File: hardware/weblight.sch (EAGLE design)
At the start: 15 parts, among them U1 ATtiny85-20SU

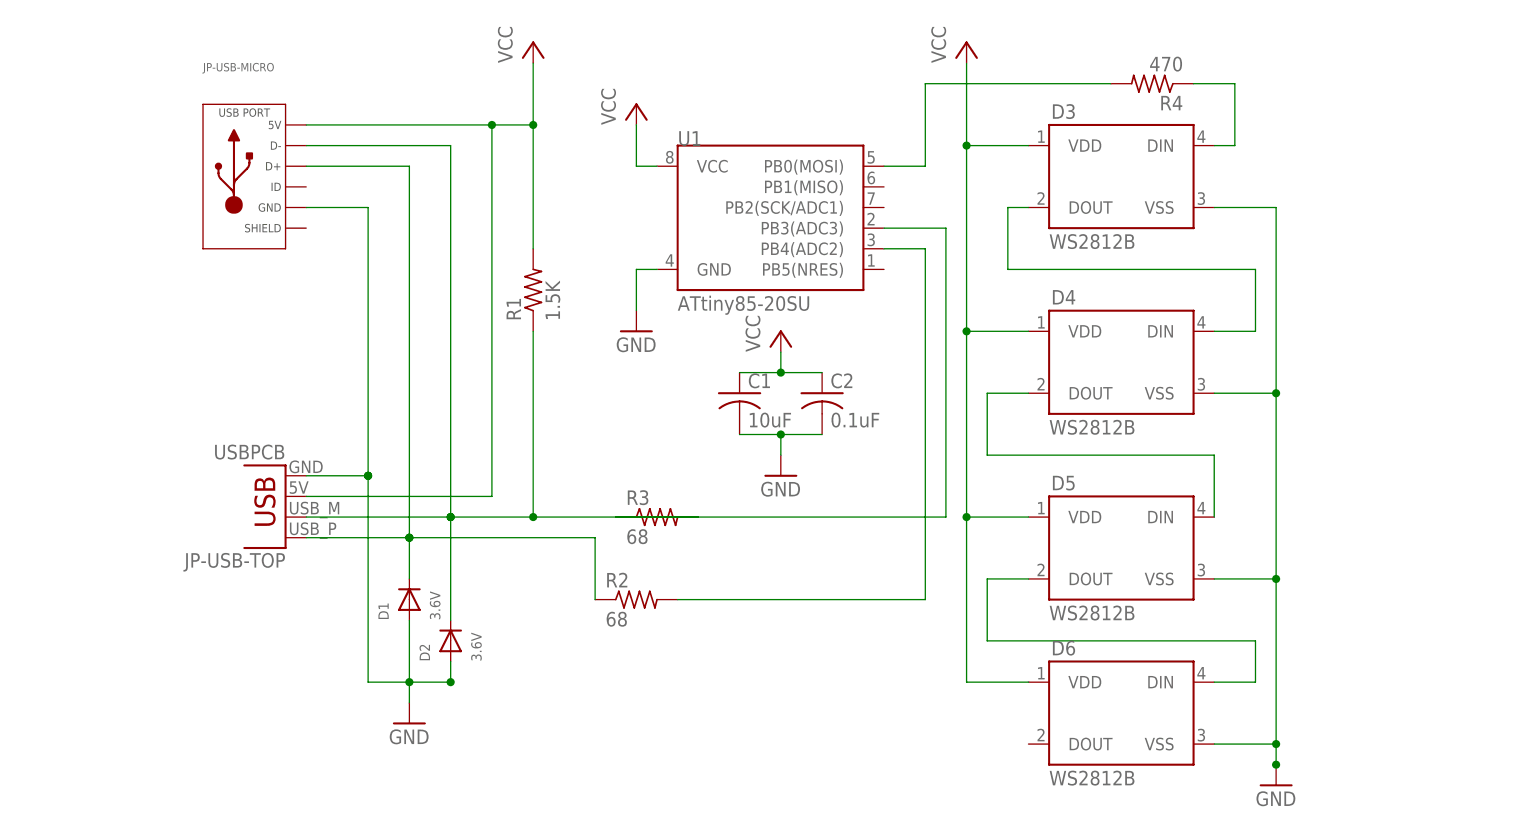
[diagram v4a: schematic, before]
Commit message: mf3 rc1
Pullup resistor on NRES
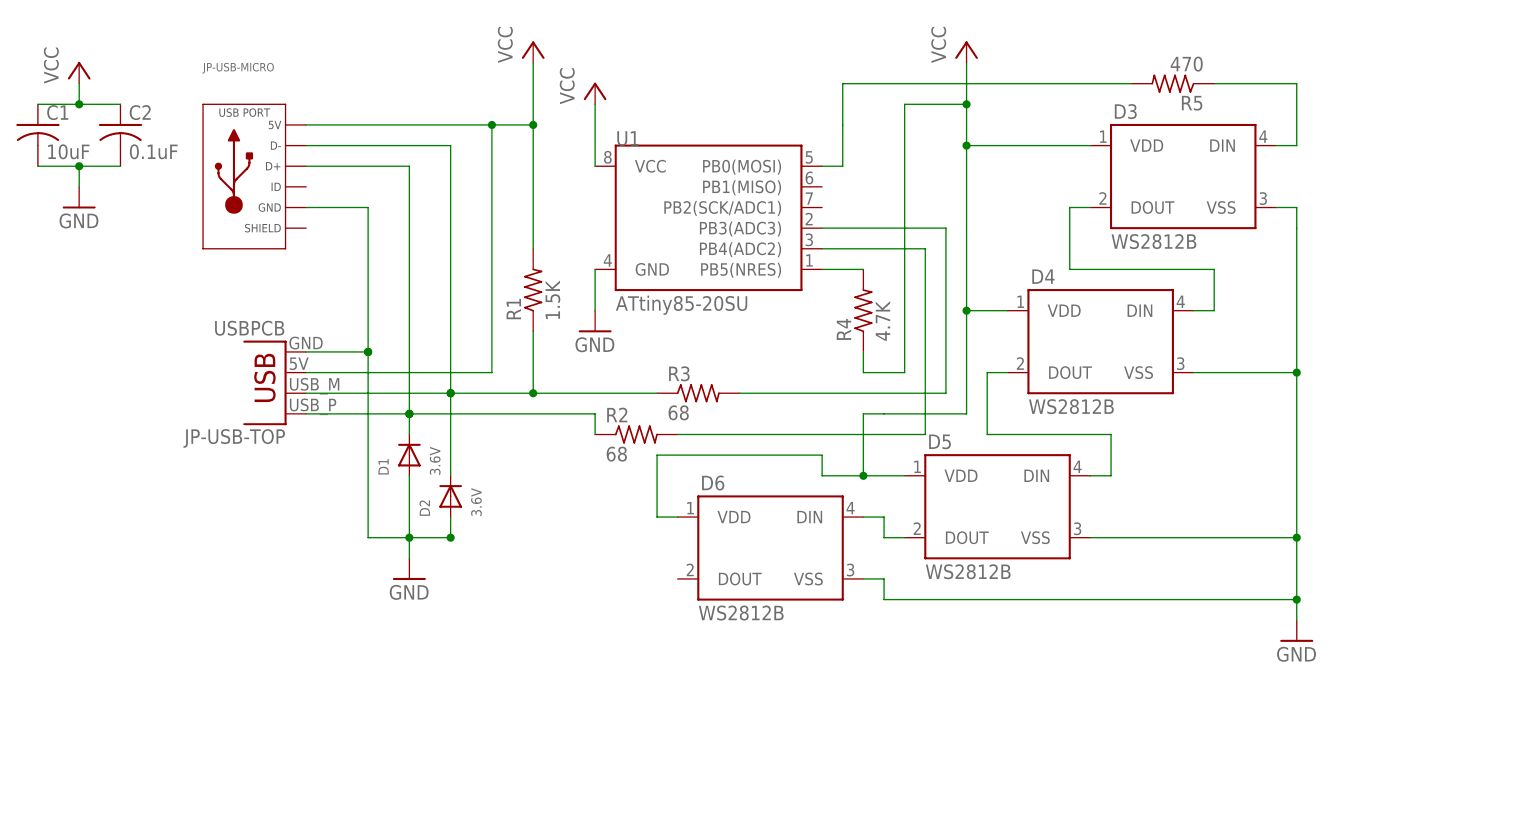
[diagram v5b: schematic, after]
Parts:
- added R5: 470, rcl:R-US_R0402
- R4: value 470 -> 4.7K
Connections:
- new net N_RESET: R4.2, U1.PB5(NRES)
- net DIN_1: now also R5.1; no longer R4.1
- net DIN_RAW: now also R5.2; no longer R4.2
- net USB_D_MINUS: now also R3.2; no longer R3.1
- net USB_D_MINUS_RAW: now also R3.1; no longer R3.2
- net VCC: now also R4.1
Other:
- moved on the sheet: C1, C2, D1, D2, D3, D4, D5, D6, JP-USB-TOP, R2, R3, R4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

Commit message: Switch over production to APA102C
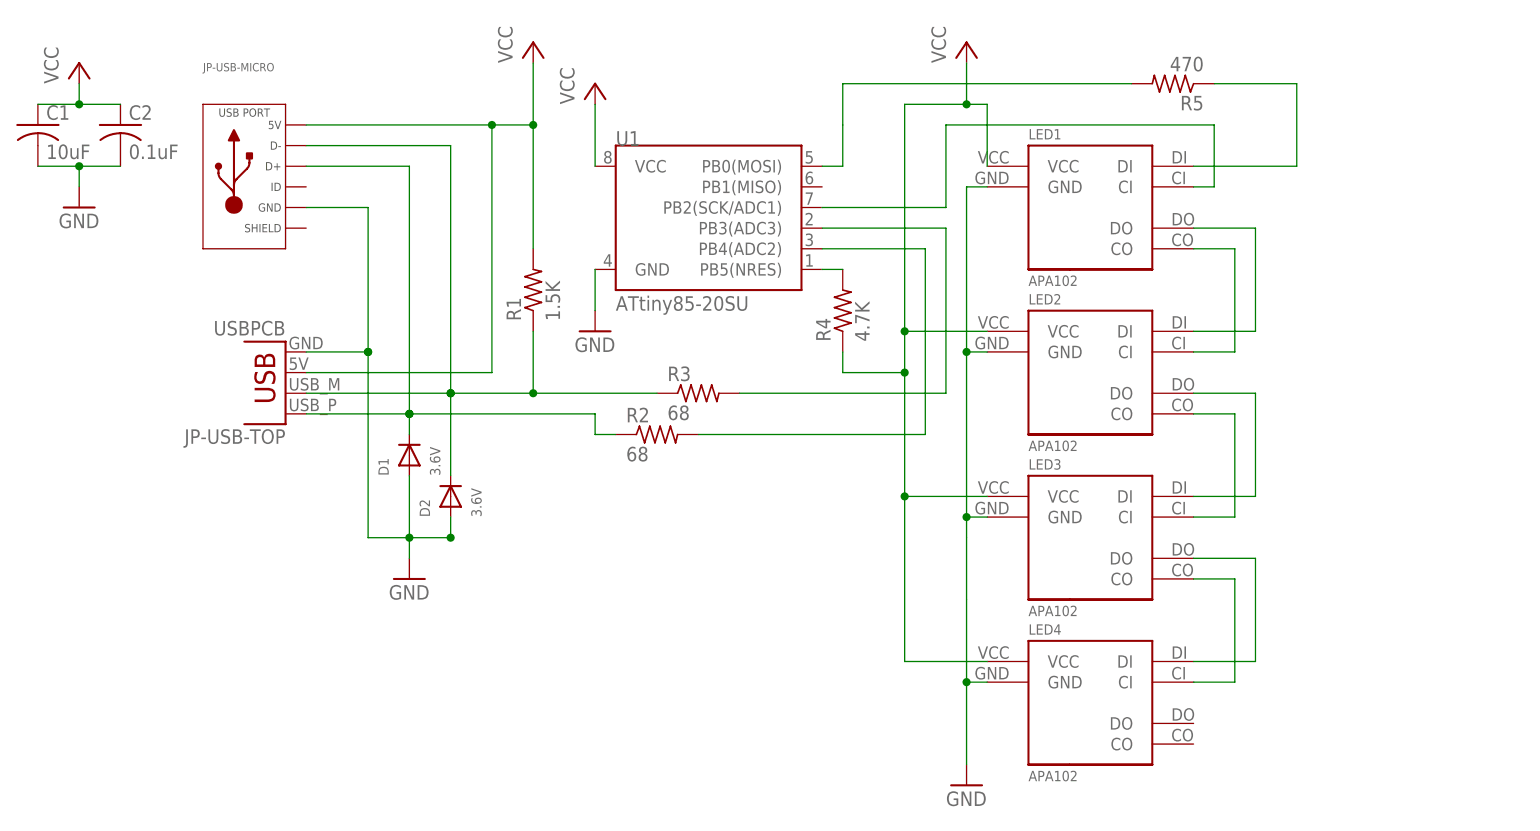
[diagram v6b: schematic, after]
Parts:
- removed D3, D4, D5, D6: WS2812B, SparkFun-LED:WS2812B
- added LED1, LED2, LED3, LED4: APA102, weblight:APA102
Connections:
- new net CLK_1: LED1.CI, U1.PB2(SCK/ADC1)
- new net CLK_2: LED1.CO, LED2.CI
- new net CLK_3: LED2.CO, LED3.CI
- new net CLK_4: LED3.CO, LED4.CI
- net DIN_1: now also LED1.DI; no longer D3.DIN
- net DIN_2: now also LED1.DO, LED2.DI; no longer D3.DOUT, D4.DIN
- net DIN_3: now also LED2.DO, LED3.DI; no longer D4.DOUT, D5.DIN
- net DIN_4: now also LED3.DO, LED4.DI; no longer D5.DOUT, D6.DIN
- net GND: now also LED1.GND, LED2.GND, LED3.GND, LED4.GND; no longer D3.VSS, D4.VSS, D5.VSS, D6.VSS
- net VCC: now also LED1.VCC, LED2.VCC, LED3.VCC, LED4.VCC; no longer D3.VDD, D4.VDD, D5.VDD, D6.VDD
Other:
- moved on the sheet: R2, R4
